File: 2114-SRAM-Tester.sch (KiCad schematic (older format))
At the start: 5 parts, among them U1 ATMEGA328P-P, U2 2114, U3 4040

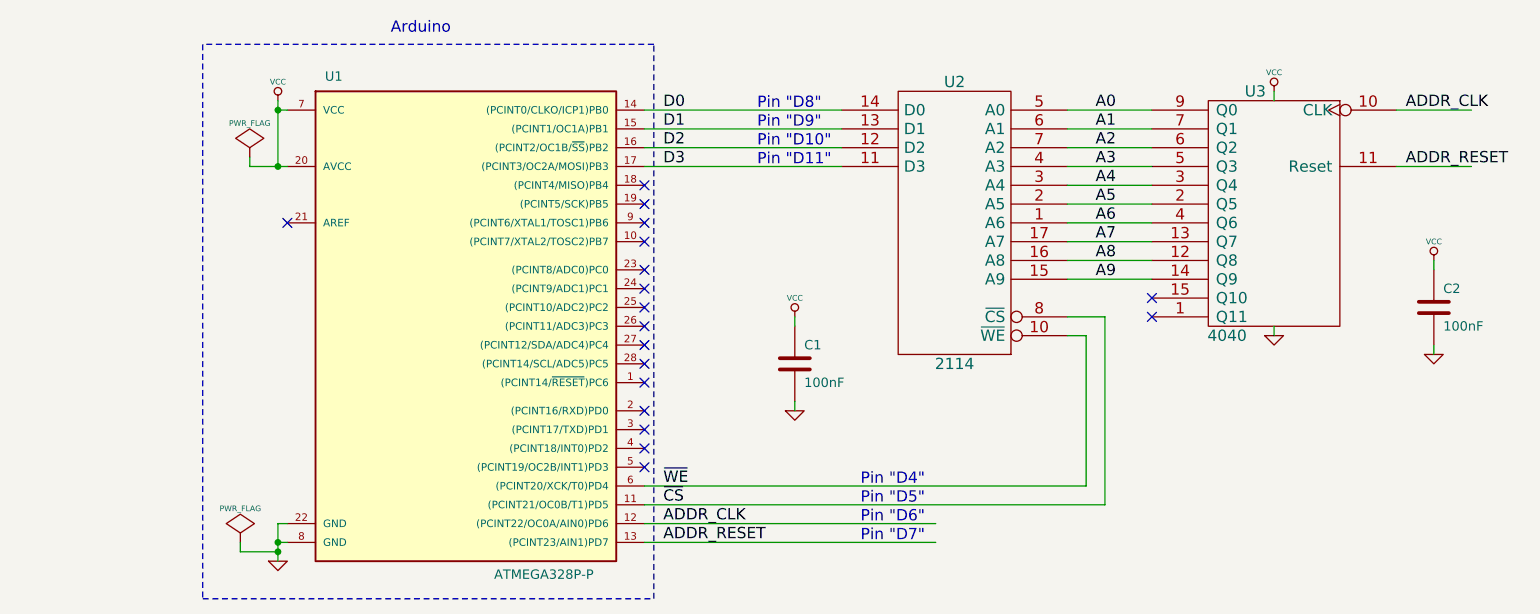
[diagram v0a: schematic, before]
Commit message: Added Arduino code
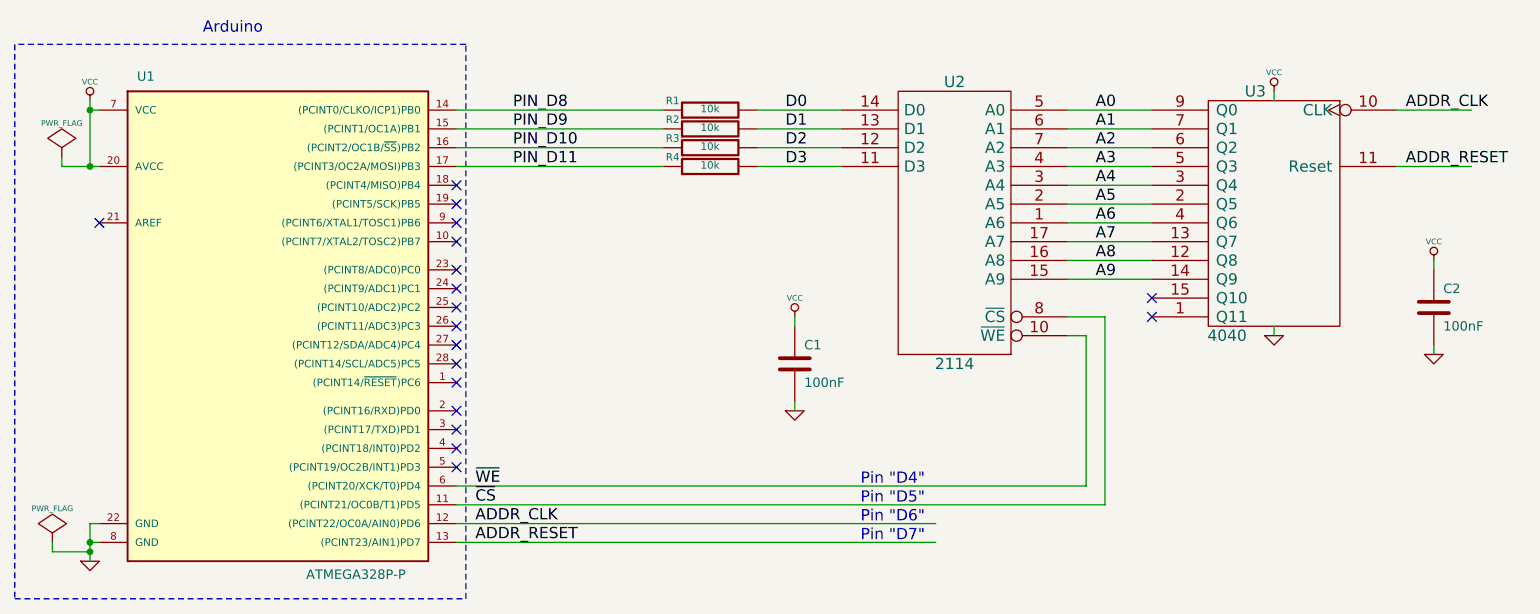
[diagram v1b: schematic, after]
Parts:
- added R1, R2, R3, R4: 10k, ~, symbol R
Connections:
- net labels added: PIN_D10, PIN_D11, PIN_D8, PIN_D9
- wire segments 39 -> 43
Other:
- note removed: "Pin "D10""
- note removed: "Pin "D11""
- note removed: "Pin "D8""
- note removed: "Pin "D9""
- moved on the sheet: U1
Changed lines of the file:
@@
 LIBS:contrib
 LIBS:valves
-LIBS:2114
 LIBS:2114-SRAM-Tester-cache
 EELAYER 24 0
@@
 Sheet 1 1
 Title "IMKO-1 Utilities"
-Date "21 may 2013"
+Date "24 may 2013"
 Rev "0.1"
 Comp "Released under the Creative Commons Attribution Share-Alike 3.0"
@@
 L ATMEGA328P-P U1
 U 1 1 506C71AF
-P 4850 4400
-F 0 "U1" H 4150 5650 50  0000 L BNN
-F 1 "ATMEGA328P-P" H 5050 3000 50  0000 L BNN
-F 2 "DIL28" H 4250 3050 50  0001 C CNN
-F 3 "" H 4850 4400 60  0001 C CNN
-	1    4850 4400
+P 3850 4400
+F 0 "U1" H 3150 5650 50  0000 L BNN
+F 1 "ATMEGA328P-P" H 4050 3000 50  0000 L BNN
+F 2 "DIL28" H 3250 3050 50  0001 C CNN
+F 3 "" H 3850 4400 60  0001 C CNN
+	1    3850 4400
 	1    0    0    -1
 $EndComp
@@
 	8550 4200 8100 4200
 Wire Wire Line
-	6900 3300 5850 3300
-Wire Wire Line
-	6900 3400 5850 3400
-Wire Wire Line
-	6900 3500 5850 3500
-Wire Wire Line
-	6900 3600 5850 3600
-Wire Wire Line
-	3950 5500 3900 5500
-Wire Wire Line
-	3900 5500 3900 5700
-Wire Wire Line
-	3900 5600 3950 5600
+	2950 5500 2900 5500
+Wire Wire Line
+	2900 5500 2900 5700
+Wire Wire Line
+	2900 5600 2950 5600
 $Comp
 L GND #PWR01
 U 1 1 506C7375
-P 3900 5700
-F 0 "#PWR01" H 3900 5700 30  0001 C CNN
-F 1 "GND" H 3900 5630 30  0001 C CNN
-F 2 "" H 3900 5700 60  0001 C CNN
-F 3 "" H 3900 5700 60  0001 C CNN
-	1    3900 5700
-	1    0    0    -1
-$EndComp
-Connection ~ 3900 5600
+P 2900 5700
+F 0 "#PWR01" H 2900 5700 30  0001 C CNN
+F 1 "GND" H 2900 5630 30  0001 C CNN
+F 2 "" H 2900 5700 60  0001 C CNN
+F 3 "" H 2900 5700 60  0001 C CNN
+	1    2900 5700
+	1    0    0    -1
+$EndComp
+Connection ~ 2900 5600
 $Comp
 L VCC #PWR02
 U 1 1 506C73A4
-P 3900 3250
-F 0 "#PWR02" H 3900 3350 30  0001 C CNN
-F 1 "VCC" H 3900 3350 30  0000 C CNN
-F 2 "" H 3900 3250 60  0001 C CNN
-F 3 "" H 3900 3250 60  0001 C CNN
-	1    3900 3250
-	1    0    0    -1
-$EndComp
-Wire Wire Line
-	3750 3600 3950 3600
-Wire Wire Line
-	3900 3250 3900 3600
-Wire Wire Line
-	3900 3300 3950 3300
-Connection ~ 3900 3300
-NoConn ~ 5850 3700
-NoConn ~ 5850 3800
-NoConn ~ 5850 3900
-NoConn ~ 5850 4000
-NoConn ~ 3950 3900
+P 2900 3250
+F 0 "#PWR02" H 2900 3350 30  0001 C CNN
+F 1 "VCC" H 2900 3350 30  0000 C CNN
+F 2 "" H 2900 3250 60  0001 C CNN
+F 3 "" H 2900 3250 60  0001 C CNN
+	1    2900 3250
+	1    0    0    -1
+$EndComp
+Wire Wire Line
+	2750 3600 2950 3600
+Wire Wire Line
+	2900 3250 2900 3600
+Wire Wire Line
+	2900 3300 2950 3300
+Connection ~ 2900 3300
+NoConn ~ 4850 3700
+NoConn ~ 4850 3800
+NoConn ~ 4850 3900
+NoConn ~ 4850 4000
+NoConn ~ 2950 3900
 $Comp
 L PWR_FLAG #FLG03
 U 1 1 506C7490
-P 3750 3550
-F 0 "#FLG03" H 3750 3645 30  0001 C CNN
-F 1 "PWR_FLAG" H 3750 3730 30  0000 C CNN
-F 2 "" H 3750 3550 60  0001 C CNN
-F 3 "" H 3750 3550 60  0001 C CNN
-	1    3750 3550
+P 2750 3550
+F 0 "#FLG03" H 2750 3645 30  0001 C CNN
+F 1 "PWR_FLAG" H 2750 3730 30  0000 C CNN
+F 2 "" H 2750 3550 60  0001 C CNN
+F 3 "" H 2750 3550 60  0001 C CNN
+	1    2750 3550
 	1    0    0    -1
 $EndComp
@@
 L PWR_FLAG #FLG04
 U 1 1 506C749D
-P 3700 5600
-F 0 "#FLG04" H 3700 5695 30  0001 C CNN
-F 1 "PWR_FLAG" H 3700 5780 30  0000 C CNN
-F 2 "" H 3700 5600 60  0001 C CNN
-F 3 "" H 3700 5600 60  0001 C CNN
-	1    3700 5600
-	1    0    0    -1
-$EndComp
-Wire Wire Line
-	3700 5600 3700 5650
-Wire Wire Line
-	3700 5650 3900 5650
-Connection ~ 3900 5650
-Wire Wire Line
-	3750 3550 3750 3600
-Connection ~ 3900 3600
+P 2700 5600
+F 0 "#FLG04" H 2700 5695 30  0001 C CNN
+F 1 "PWR_FLAG" H 2700 5780 30  0000 C CNN
+F 2 "" H 2700 5600 60  0001 C CNN
+F 3 "" H 2700 5600 60  0001 C CNN
+	1    2700 5600
+	1    0    0    -1
+$EndComp
+Wire Wire Line
+	2700 5600 2700 5650
+Wire Wire Line
+	2700 5650 2900 5650
+Connection ~ 2900 5650
+Wire Wire Line
+	2750 3550 2750 3600
+Connection ~ 2900 3600
 $Comp
 L GND #PWR05
@@
 Wire Wire Line
 	9200 3200 9200 3250
-Text Label 5950 3300 0    60   ~ 0
+Text Label 6600 3300 0    60   ~ 0
 D0
-Text Label 5950 3400 0    60   ~ 0
+Text Label 6600 3400 0    60   ~ 0
 D1
-Text Label 5950 3500 0    60   ~ 0
+Text Label 6600 3500 0    60   ~ 0
 D2
-Text Label 5950 3600 0    60   ~ 0
+Text Label 6600 3600 0    60   ~ 0
 D3
 Wire Wire Line
@@
 ADDR_RESET
 Wire Wire Line
-	5850 5600 7400 5600
-Wire Wire Line
-	5850 5500 7400 5500
-Text Label 5950 5500 0    60   ~ 0
+	4850 5600 7400 5600
+Wire Wire Line
+	4850 5500 7400 5500
+Text Label 4950 5500 0    60   ~ 0
 ADDR_CLK
-Text Label 5950 5600 0    60   ~ 0
+Text Label 4950 5600 0    60   ~ 0
 ADDR_RESET
 Wire Wire Line
@@
 	8300 4400 8300 5400
 Wire Wire Line
-	8300 5400 5850 5400
-Text Label 5950 5400 0    60   ~ 0
+	8300 5400 4850 5400
+Text Label 4950 5400 0    60   ~ 0
 ~CS
-NoConn ~ 5850 4550
-NoConn ~ 5850 4650
-NoConn ~ 5850 4750
-NoConn ~ 5850 4900
-NoConn ~ 5850 5000
-NoConn ~ 5850 5100
-NoConn ~ 5850 5200
+NoConn ~ 4850 4550
+NoConn ~ 4850 4650
+NoConn ~ 4850 4750
+NoConn ~ 4850 4900
+NoConn ~ 4850 5000
+NoConn ~ 4850 5100
+NoConn ~ 4850 5200
 Wire Notes Line
-	5900 5900 5900 2950
+	4900 5900 4900 2950
 Wire Notes Line
-	5900 2950 3500 2950
+	4900 2950 2500 2950
 Wire Notes Line
-	3500 2950 3500 5900
+	2500 2950 2500 5900
 Wire Notes Line
-	3500 5900 5900 5900
-Text Notes 4500 2900 0    60   ~ 0
+	2500 5900 4900 5900
+Text Notes 3500 2900 0    60   ~ 0
 Arduino
 Text Label 8250 3300 0    60   ~ 0
@@
 NoConn ~ 8550 4300
 NoConn ~ 8550 4400
-NoConn ~ 5850 4150
-NoConn ~ 5850 4250
-NoConn ~ 5850 4350
-NoConn ~ 5850 4450
-Wire Wire Line
-	5850 5300 8200 5300
+NoConn ~ 4850 4150
+NoConn ~ 4850 4250
+NoConn ~ 4850 4350
+NoConn ~ 4850 4450
+Wire Wire Line
+	4850 5300 8200 5300
 Wire Wire Line
 	8200 5300 8200 4500
 Wire Wire Line
 	8200 4500 8100 4500
-Text Label 5950 5300 0    60   ~ 0
+Text Label 4950 5300 0    60   ~ 0
 ~WE
 Text Notes 7000 5300 0    60   ~ 0
@@
 Text Notes 7000 5600 0    60   ~ 0
 Pin "D7"
-Text Notes 6450 3300 0    60   ~ 0
-Pin "D8"
-Text Notes 6450 3400 0    60   ~ 0
-Pin "D9"
-Text Notes 6450 3500 0    60   ~ 0
-Pin "D10"
-Text Notes 6450 3600 0    60   ~ 0
-Pin "D11"
+$Comp
+L R R1
+U 1 1 519F4F26
+P 6200 3300
+F 0 "R1" V 6250 3500 40  0000 C CNN
+F 1 "10k" V 6207 3301 40  0000 C CNN
+F 2 "~" V 6130 3300 30  0000 C CNN
+F 3 "~" H 6200 3300 30  0000 C CNN
+	1    6200 3300
+	0    -1   -1   0
+$EndComp
+$Comp
+L R R2
+U 1 1 519F4F33
+P 6200 3400
+F 0 "R2" V 6250 3600 40  0000 C CNN
+F 1 "10k" V 6207 3401 40  0000 C CNN
+F 2 "~" V 6130 3400 30  0000 C CNN
+F 3 "~" H 6200 3400 30  0000 C CNN
+	1    6200 3400
+	0    -1   -1   0
+$EndComp
+$Comp
+L R R3
+U 1 1 519F4F39
+P 6200 3500
+F 0 "R3" V 6250 3700 40  0000 C CNN
+F 1 "10k" V 6207 3501 40  0000 C CNN
+F 2 "~" V 6130 3500 30  0000 C CNN
+F 3 "~" H 6200 3500 30  0000 C CNN
+	1    6200 3500
+	0    -1   -1   0
+$EndComp
+$Comp
+L R R4
+U 1 1 519F4F3F
+P 6200 3600
+F 0 "R4" V 6250 3800 40  0000 C CNN
+F 1 "10k" V 6207 3601 40  0000 C CNN
+F 2 "~" V 6130 3600 30  0000 C CNN
+F 3 "~" H 6200 3600 30  0000 C CNN
+	1    6200 3600
+	0    -1   -1   0
+$EndComp
+Wire Wire Line
+	6450 3300 6900 3300
+Wire Wire Line
+	5950 3300 4850 3300
+Wire Wire Line
+	4850 3400 5950 3400
+Wire Wire Line
+	5950 3500 4850 3500
+Wire Wire Line
+	4850 3600 5950 3600
+Wire Wire Line
+	6450 3400 6900 3400
+Wire Wire Line
+	6450 3500 6900 3500
+Wire Wire Line
+	6450 3600 6900 3600
+Text Label 5150 3300 0    60   ~ 0
+PIN_D8
+Text Label 5150 3400 0    60   ~ 0
+PIN_D9
+Text Label 5150 3500 0    60   ~ 0
+PIN_D10
+Text Label 5150 3600 0    60   ~ 0
+PIN_D11
 $EndSCHEMATC
